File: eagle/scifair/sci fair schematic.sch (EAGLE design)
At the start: 12 parts, among them IC1 LM555N, Q1 BC817-16W, Q2 BC817-16W, Q3 BC817-16W, X1 RIGHT, X2 LEFT, X3 PWR

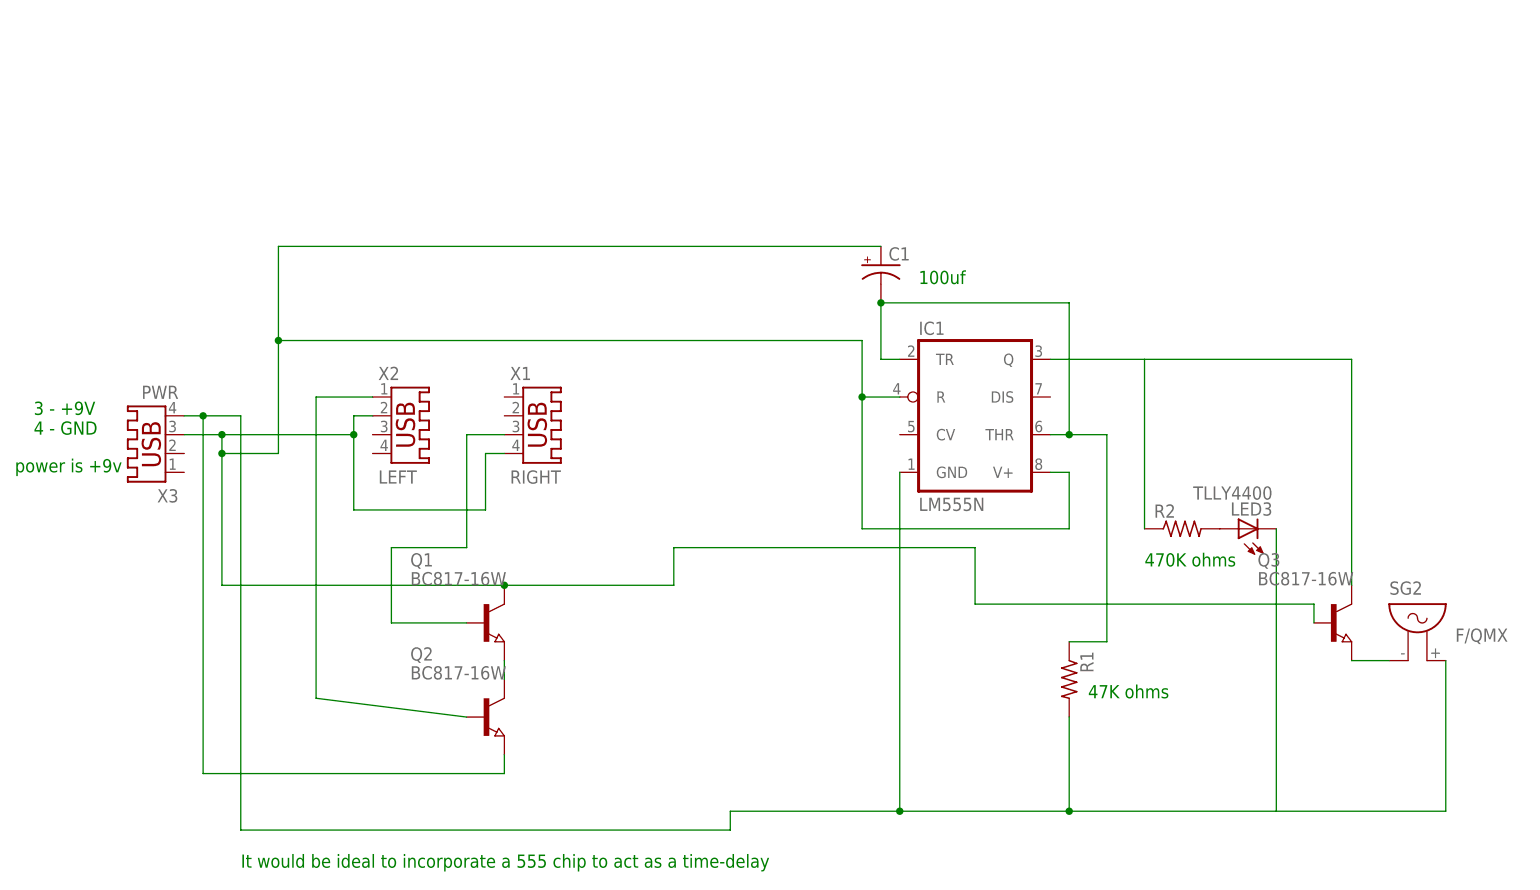
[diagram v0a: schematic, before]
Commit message: Rework design in entirety to solve issues with previous design
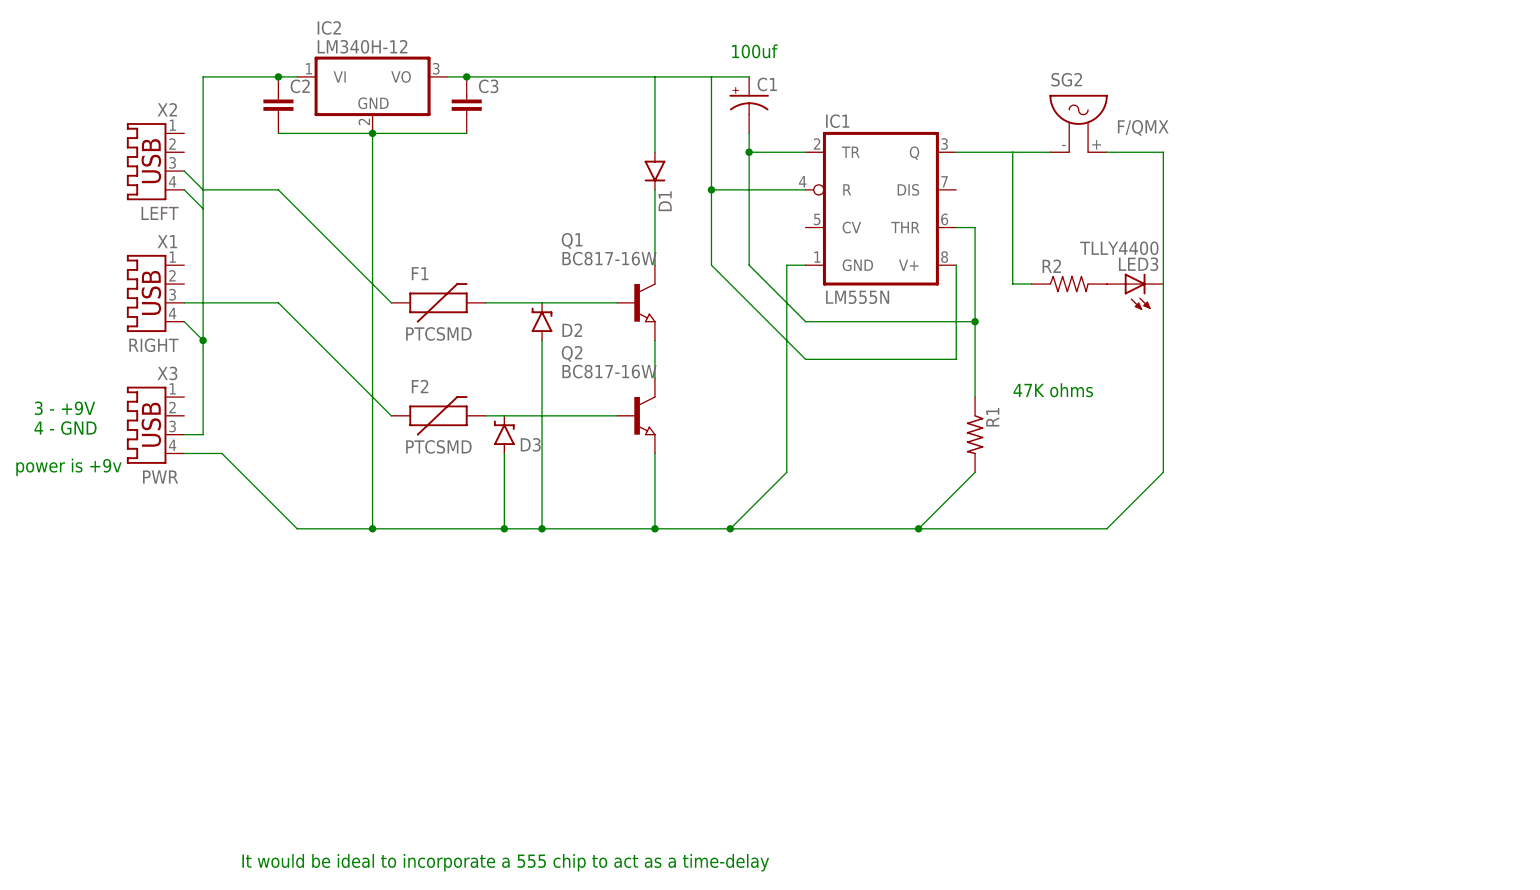
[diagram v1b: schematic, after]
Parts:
- removed Q3: BC817-16W, semicon-smd-ipc:NPN-TRANSISTOR_SOT23
- added C2, C3: (no value), capacitor-wima:C5/2.5
- added D1: (no value), SparkFun-DiscreteSemi:DIODEPTH
- added D2, D3: DIODE-ZENERPTH, SparkFun-DiscreteSemi:DIODE-ZENERPTH
- added F1, F2: PTCSMD, SparkFun-PowerIC:PTCSMD
- added IC2: LM340H-12, linear:LM340H-12
- R2: device rcl:R-US_0207/12 -> SparkFun-Passives:RESISTORPTH-1/2W
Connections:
- new net N$1: C2.1, IC2.VI, X1.4, X2.4, X3.3
- new net N$10: IC1.Q, R2.1, SG2.1
- new net N$5: C2.2, C3.2, D2.A, D3.A, IC1.GND, IC2.GND, LED3.C, Q2.E, R1.2, SG2.2, X3.4
- net N$2: now also F1.1, X2.3; no longer Q1.B, X1.3
- net N$3: now also F2.1, X1.3; no longer Q2.B, X2.1
- net N$6: now also C1.+, C3.1, D1.A, IC1.R, IC1.V+, IC2.VO; no longer Q3.E, SG2.1
- net N$7: now also D1.C, Q1.C; no longer IC1.GND, LED3.C, Q2.E, R1.2, SG2.2, X3.4
- net N$8: now also D2.C, F1.2, Q1.B; no longer C1.+, IC1.R, IC1.V+, Q1.C, Q3.B, X1.4, X2.2, X3.3
- net N$9: now also D3.C, F2.2, Q2.B; no longer IC1.Q, Q3.C, R2.1
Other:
- note removed: "470K ohms"
- moved on the sheet: C1, IC1, LED3, Q1, Q2, R1, R2, SG2, X1, X2, X3
